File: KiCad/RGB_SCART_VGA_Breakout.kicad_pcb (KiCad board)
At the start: 2 copper layers, 81 x 40.5 mm, 23 parts, among them J1 SCART-F, J11 SJ1-3535NG, J3 DE15_Plug_HighDensity_Mountin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, J4 Conn_01x09, J5 Mounting, J6 Mounting, J7 Mounting, J8 Mounting

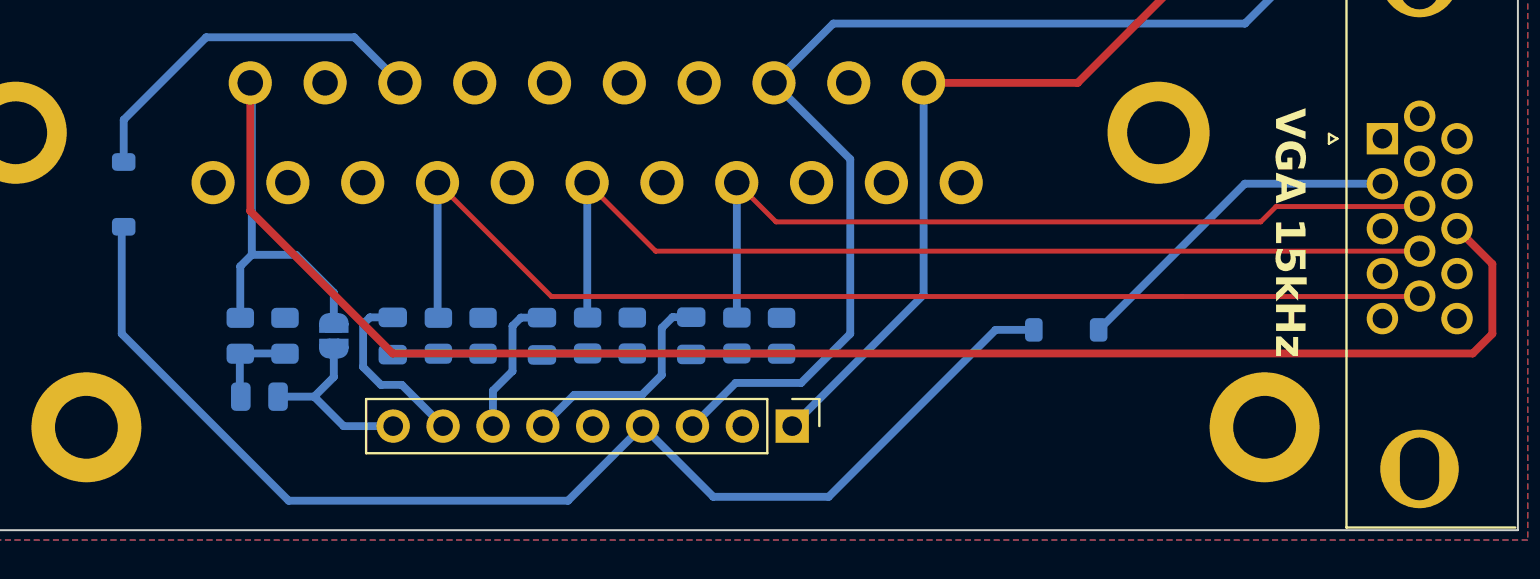
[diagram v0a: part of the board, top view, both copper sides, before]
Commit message: Fixed DE15/VGA connector pinout.
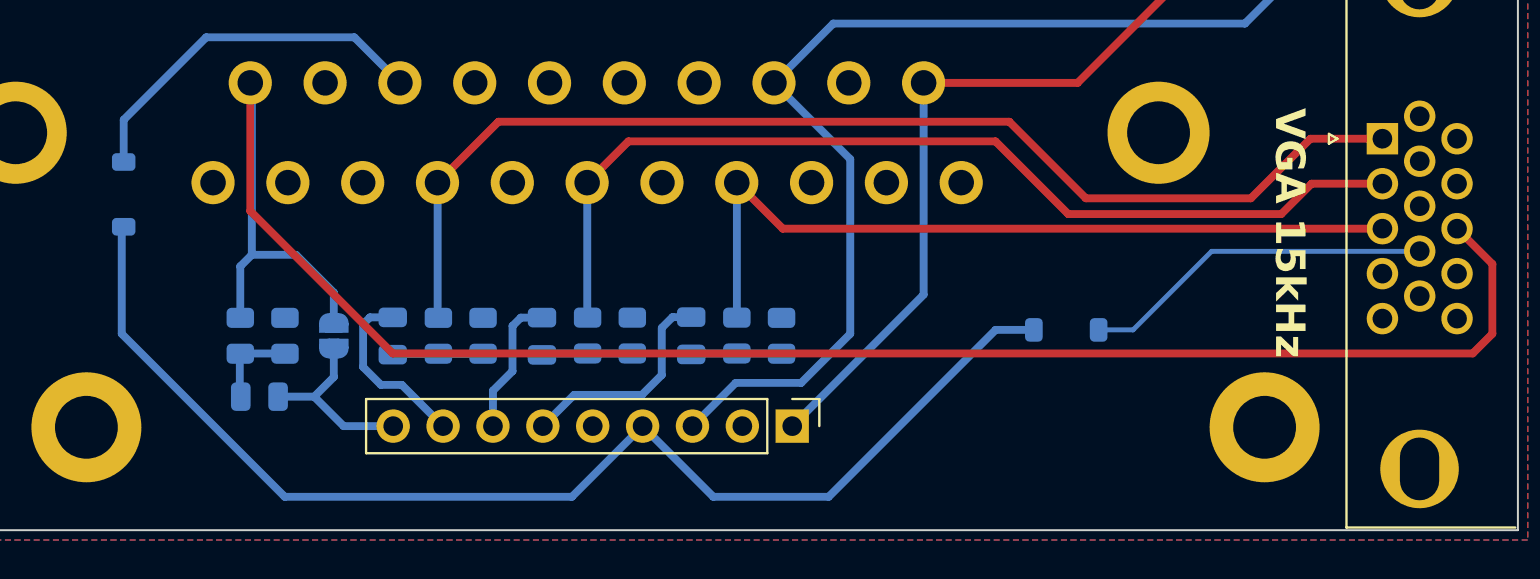
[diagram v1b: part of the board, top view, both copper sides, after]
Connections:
- J3 pad 1: GND -> /RED
- J3 pad 10: /RED -> GND
- J3 pad 12: /VGA_V_SYNC -> unconnected-(J3-Pad12)
- J3 pad 14: unconnected-(J3-Pad14) -> /VGA_V_SYNC
- J3 pad 2: /VGA_5V -> /GREEN
- J3 pad 3: GND -> /BLUE
- J3 pad 4: GND -> unconnected-(J3-Pad4)
- J3 pad 7: unconnected-(J3-Pad7) -> GND
- J3 pad 8: /BLUE -> GND
- J3 pad 9: /GREEN -> /VGA_5V
- J3 pad SH: unconnected-(J3-PadSH)_1 -> (no net)
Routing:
- net /BLUE: track 42.8 -> 40.7 mm
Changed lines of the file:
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@@
 			)
 		)
-		(property "Description" "15-pin D-SUB connector, socket (female), High density (3 columns), Triple Row, Generic, VGA-connector, Mounting Hole"
+		(property "Description" "15-pin D-SUB connector, socket (female), High density (3 columns), Triple Row, Generic, VGA-connector"
 			(at 0 0 90)
 			(layer "F.Fab")
@@
 			(unit
 				(name "A")
-				(pins "6" "1" "7" "2" "8" "3" "9" "4" "10" "5" "SH" "11" "12" "13" "14"
-					"15"
-				)
+				(pins "6" "1" "7" "2" "8" "3" "9" "4" "10" "5" "11" "12" "13" "14" "15")
 			)
 		)
@@
 			(layers "*.Cu" "*.Mask")
 			(remove_unused_layers no)
-			(net "GND")
+			(net "/RED")
 			(pintype "passive")
 		)
@@
 			(layers "*.Cu" "*.Mask")
 			(remove_unused_layers no)
-			(net "/VGA_5V")
+			(net "/GREEN")
 			(pintype "passive")
 		)
@@
 			(layers "*.Cu" "*.Mask")
 			(remove_unused_layers no)
-			(net "GND")
+			(net "/BLUE")
 			(pintype "passive")
 		)
@@
 			(layers "*.Cu" "*.Mask")
 			(remove_unused_layers no)
-			(net "GND")
-			(pintype "passive")
+			(net "unconnected-(J3-Pad4)")
+			(pintype "passive+no_connect")
 		)
 		(pad "5" thru_hole circle
@@
 			(layers "*.Cu" "*.Mask")
 			(remove_unused_layers no)
-			(net "unconnected-(J3-Pad7)")
-			(pintype "passive+no_connect")
+			(net "GND")
+			(pintype "passive")
 		)
 		(pad "8" thru_hole circle
@@
 			(layers "*.Cu" "*.Mask")
 			(remove_unused_layers no)
-			(net "/BLUE")
+			(net "GND")
 			(pintype "passive")
 		)
@@
 			(layers "*.Cu" "*.Mask")
 			(remove_unused_layers no)
-			(net "/GREEN")
+			(net "/VGA_5V")
 			(pintype "passive")
 		)
@@
 			(layers "*.Cu" "*.Mask")
 			(remove_unused_layers no)
-			(net "/RED")
+			(net "GND")
 			(pintype "passive")
 		)
@@
 			(layers "*.Cu" "*.Mask")
 			(remove_unused_layers no)
-			(net "/VGA_V_SYNC")
+			(net "unconnected-(J3-Pad12)")
 			(pintype "passive+no_connect")
 		)
@@
 			(layers "*.Cu" "*.Mask")
 			(remove_unused_layers no)
-			(net "unconnected-(J3-Pad14)")
-			(pintype "passive+no_connect")
+			(net "/VGA_V_SYNC")
+			(pintype "passive")
 		)
 		(pad "15" thru_hole circle
@@
 			(layers "*.Cu" "*.Mask")
 			(remove_unused_layers no)
-			(net "unconnected-(J3-PadSH)")
-			(pintype "passive+no_connect")
 		)
 		(pad "SH" thru_hole circle
@@
 			(layers "*.Cu" "*.Mask")
 			(remove_unused_layers no)
-			(net "unconnected-(J3-PadSH)_1")
-			(pintype "passive+no_connect")
 		)
 		(embedded_fonts no)
@@
 	)
 	(segment
+		(start 191.2 87.8)
+		(end 191.18 87.82)
+		(width 0.25)
+		(layer "F.Cu")
+		(net "GND")
+	)
+	(segment
 		(start 156.679 98.9965)
 		(end 156.679 98.3615)
@@
 	)
 	(segment
+		(start 191.2 92.38)
+		(end 191.18 92.4)
+		(width 0.25)
+		(layer "F.Cu")
+		(net "GND")
+	)
+	(segment
 		(start 156.679 98.9965)
 		(end 156.679 98.933)
@@
 	)
 	(segment
-		(start 147.8245 102.8)
+		(start 148.0245 102.6)
 		(end 151.6245 99)
 		(width 0.4)
@@
 	)
 	(segment
-		(start 125.1 88.95)
-		(end 125.1 94.3)
+		(start 133.4 102.6)
+		(end 148.0245 102.6)
 		(width 0.4)
 		(layer "B.Cu")
@@
 	)
 	(segment
-		(start 125.1 94.3)
-		(end 133.6 102.8)
+		(start 125.1 88.95)
+		(end 125.1 94.3)
 		(width 0.4)
 		(layer "B.Cu")
@@
 	)
 	(segment
-		(start 133.6 102.8)
-		(end 147.8245 102.8)
+		(start 151.599 98.9965)
+		(end 151.599 98.8695)
 		(width 0.4)
 		(layer "B.Cu")
@@
 	)
 	(segment
-		(start 151.599 98.9965)
-		(end 151.599 98.8695)
+		(start 125.1 94.3)
+		(end 133.4 102.6)
 		(width 0.4)
 		(layer "B.Cu")
@@
 	)
 	(segment
-		(start 182.295 86.655)
-		(end 174.85 94.1)
+		(start 144.28 83.5)
+		(end 170.3 83.5)
 		(width 0.4)
-		(layer "B.Cu")
-		(net "/VGA_5V")
+		(layer "F.Cu")
+		(net "/RED")
 	)
 	(segment
-		(start 189.3 86.655)
-		(end 182.295 86.655)
+		(start 141.18 86.6)
+		(end 144.28 83.5)
 		(width 0.4)
-		(layer "B.Cu")
-		(net "/VGA_5V")
-	)
-	(segment
-		(start 191.2 87.8)
-		(end 191.18 87.82)
-		(width 0.25)
 		(layer "F.Cu")
-		(net "/BLUE")
+		(net "/RED")
 	)
 	(segment
-		(start 183.88 87.82)
-		(end 183.1 88.6)
-		(width 0.25)
+		(start 185.635 84.365)
+		(end 189.3 84.365)
+		(width 0.4)
 		(layer "F.Cu")
-		(net "/BLUE")
+		(net "/RED")
 	)
 	(segment
-		(start 158.42 88.6)
-		(end 156.42 86.6)
-		(width 0.25)
+		(start 182.6 87.4)
+		(end 185.635 84.365)
+		(width 0.4)
 		(layer "F.Cu")
-		(net "/BLUE")
+		(net "/RED")
 	)
 	(segment
-		(start 183.1 88.6)
-		(end 158.42 88.6)
-		(width 0.25)
+		(start 174.2 87.4)
+		(end 182.6 87.4)
+		(width 0.4)
 		(layer "F.Cu")
-		(net "/BLUE")
+		(net "/RED")
 	)
 	(segment
-		(start 191.18 87.82)
-		(end 183.88 87.82)
-		(width 0.25)
+		(start 170.3 83.5)
+		(end 174.2 87.4)
+		(width 0.4)
 		(layer "F.Cu")
-		(net "/BLUE")
+		(net "/RED")
 	)
 	(segment
-		(start 156.425 86.605)
-		(end 156.42 86.6)
+		(start 141.185 93.411)
+		(end 141.185 86.605)
 		(width 0.4)
 		(layer "B.Cu")
-		(net "/BLUE")
+		(net "/RED")
 	)
 	(segment
-		(start 156.425 93.4755)
-		(end 156.425 86.605)
+		(start 141.185 86.605)
+		(end 141.18 86.6)
 		(width 0.4)
 		(layer "B.Cu")
-		(net "/BLUE")
+		(net "/RED")
 	)
 	(segment
-		(start 152.29 90.09)
-		(end 148.8 86.6)
-		(width 0.25)
+		(start 169.6 84.5)
+		(end 173.3 88.2)
+		(width 0.4)
 		(layer "F.Cu")
 		(net "/GREEN")
 	)
 	(segment
-		(start 191.2 90.09)
-		(end 152.29 90.09)
-		(width 0.25)
+		(start 148.8 86.6)
+		(end 150.9 84.5)
+		(width 0.4)
+		(layer "F.Cu")
+		(net "/GREEN")
+	)
+	(segment
+		(start 184.15 88.2)
+		(end 185.695 86.655)
+		(width 0.4)
+		(layer "F.Cu")
+		(net "/GREEN")
+	)
+	(segment
+		(start 173.3 88.2)
+		(end 184.15 88.2)
+		(width 0.4)
+		(layer "F.Cu")
+		(net "/GREEN")
+	)
+	(segment
+		(start 150.9 84.5)
+		(end 169.6 84.5)
+		(width 0.4)
+		(layer "F.Cu")
+		(net "/GREEN")
+	)
+	(segment
+		(start 185.695 86.655)
+		(end 189.3 86.655)
+		(width 0.4)
 		(layer "F.Cu")
 		(net "/GREEN")
@@
 	)
 	(segment
-		(start 179.1 92.4)
-		(end 146.98 92.4)
-		(width 0.25)
+		(start 189.3 88.945)
+		(end 158.765 88.945)
+		(width 0.4)
 		(layer "F.Cu")
-		(net "/RED")
+		(net "/BLUE")
 	)
 	(segment
-		(start 191.2 92.38)
-		(end 191.18 92.4)
-		(width 0.25)
+		(start 158.765 88.945)
+		(end 156.42 86.6)
+		(width 0.4)
 		(layer "F.Cu")
-		(net "/RED")
+		(net "/BLUE")
 	)
 	(segment
-		(start 146.98 92.4)
-		(end 141.18 86.6)
+		(start 156.425 86.605)
+		(end 156.42 86.6)
+		(width 0.4)
+		(layer "B.Cu")
+		(net "/BLUE")
+	)
+	(segment
+		(start 156.425 93.4755)
+		(end 156.425 86.605)
+		(width 0.4)
+		(layer "B.Cu")
+		(net "/BLUE")
+	)
+	(segment
+		(start 180.6 90.1)
+		(end 176.6 94.1)
 		(width 0.25)
-		(layer "F.Cu")
-		(net "/RED")
+		(layer "B.Cu")
+		(net "/VGA_5V")
 	)
 	(segment
-		(start 191.18 92.4)
-		(end 179.1 92.4)
+		(start 191.19 90.1)
+		(end 180.6 90.1)
 		(width 0.25)
-		(layer "F.Cu")
-		(net "/RED")
+		(layer "B.Cu")
+		(net "/VGA_5V")
 	)
 	(segment
-		(start 141.185 93.411)
-		(end 141.185 86.605)
-		(width 0.4)
+		(start 191.2 90.09)
+		(end 191.19 90.1)
+		(width 0.25)
 		(layer "B.Cu")
-		(net "/RED")
+		(net "/VGA_5V")
 	)
 	(segment
-		(start 141.185 86.605)
-		(end 141.18 86.6)
-		(width 0.4)
+		(start 176.6 94.1)
+		(end 174.85 94.1)
+		(width 0.25)
 		(layer "B.Cu")
-		(net "/RED")
+		(net "/VGA_5V")
 	)
 	(segment

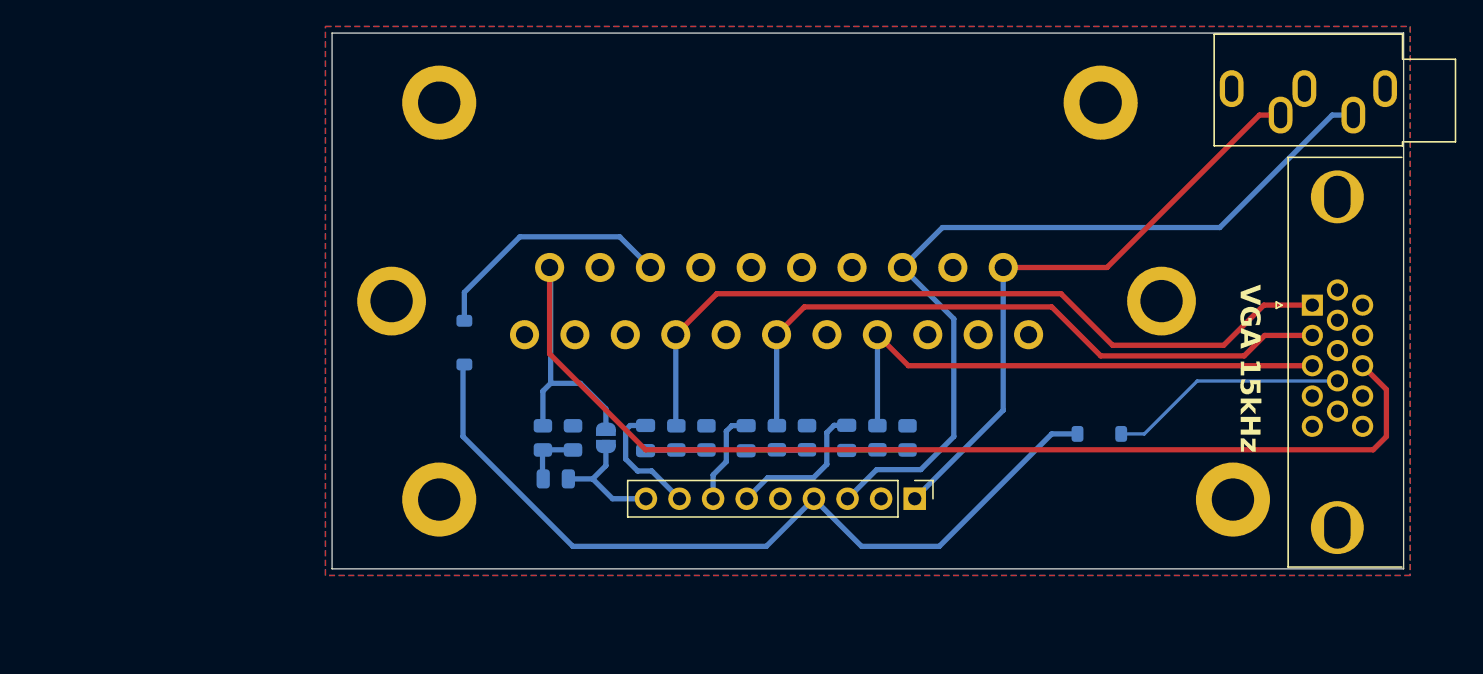
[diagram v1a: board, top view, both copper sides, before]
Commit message: Implement SCART/VGA/S-Video breakout board for JVC TM-1011G RGB/S-Video mod.
MiniDIN 4 pin connector 3D model obtained from https://grabcad.com/library/din-4-pin-connector-2
MiniDIN 4 pin connector footprint edited from MiniDIN 6 pin https://github.com/4x1md/kicad_libraries/blob/master/Custom_Footprints.pretty/Connector_Mini-DIN_Female_6Pin_2rows.kicad_mod
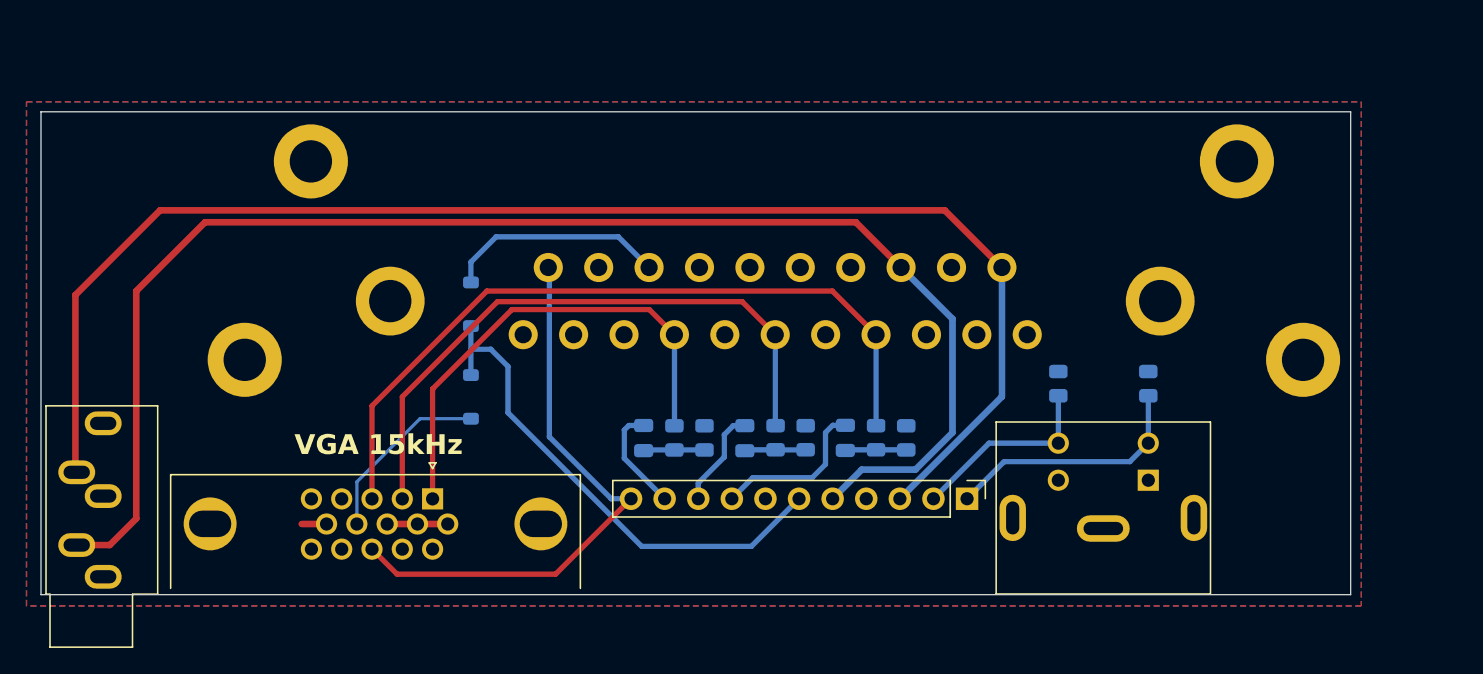
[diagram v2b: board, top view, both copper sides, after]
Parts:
- removed C4: 100nF, Capacitor_SMD:C_0805_2012Metric
- removed JP1: SolderJumper_2_Open, Jumper:SolderJumper-2_P1.3mm_Open_RoundedPad1.0x1.5mm
- removed R4: 30R, Resistor_SMD:R_0805_2012Metric
- removed R5: 75R, Resistor_SMD:R_0805_2012Metric
- added J2: Mini-DIN-4, Connector_Mini-DIN:Connector_Mini-DIN_Female_4Pin, F.Cu at (174.8, 97.6)
- added R10: 510R, Resistor_SMD:R_0805_2012Metric, B.Cu at (170.1, 90.3)
- added R9: 510R, Resistor_SMD:R_0805_2012Metric, B.Cu at (176.9, 90.3)
- J4: footprint Connector_PinHeader_2.54mm:PinHeader_1x09_P2.54mm_Vertical -> Connector_PinHeader_2.54mm:PinHeader_1x11_P2.54mm_Vertical
- moved J11 103.7 mm to (97.9, 104.9), turned to 180 degrees
- moved J3 68.1 mm to (122.8, 99.0), turned to 0 degrees
- moved D1 47.6 mm to (125.7, 91.3), turned to -90 degrees
- moved J6 18.1 mm to (108.6, 88.5)
- moved J5 11.8 mm to (188.6, 88.5)
- moved J8 11.2 mm to (183.6, 73.5)
- moved J7 10.7 mm to (113.6, 73.5)
- moved J4 3.96 mm to (163.2, 99.0)
- moved D2 2.94 mm to (125.7, 84.3)
- moved C1 0.15 mm to (138.8, 94.4)
- moved R1 0.15 mm to (141.1, 94.4)
- moved R8 0.15 mm to (143.4, 94.4)
- moved J1 0.10 mm to (148.7, 84.1)
- moved R3 0.10 mm to (156.3, 94.4)
- moved C2 0.10 mm to (146.4, 94.4)
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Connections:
- J4 pad 1: /AUDIO_R -> /LUMA
- J4 pad 2: GND -> /CHROMA
- J4 pad 3: /AUDIO_L -> /AUDIO_R
- J4 pad 4: /BLANKING -> GND
- J4 pad 5: GND -> /AUDIO_L
- J4 pad 6: /BLUE_OUT -> /BLANKING
- J4 pad 7: /GREEN_OUT -> GND
- J4 pad 8: /RED_OUT -> /BLUE_OUT
- J4 pad 9: /CSYNC_OUT -> /GREEN_OUT
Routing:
- net /AUDIO_R: track 46.0 -> 108.6 mm
- net /CSYNC: track 98.1 -> 43.7 mm
- net /AUDIO_L: track 63.2 -> 109.1 mm
- net /BLANKING: track 62.0 -> 38.2 mm
- net /RED: track 59.1 -> 36.7 mm
- net /LUMA: track 0.00 -> 19.0 mm
- net /BLUE: track 40.7 -> 57.0 mm
- net /CHROMA: track 0.00 -> 14.8 mm
- net /CSYNC_OUT: track 9.47 -> 0.00 mm
- net GND: track 0.76 -> 6.45 mm
- net Net-(C4-Pad2): track 4.33 -> 0.00 mm
- net /VGA_5V: track 18.0 -> 13.8 mm
- net /GREEN: track 50.4 -> 46.7 mm
- net Net-(D2-A): track 18.9 -> 16.8 mm
- net /RED_OUT: track 9.41 -> 8.11 mm
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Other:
- board size 81 x 40.5 mm -> 99 x 36.5 mm
- board text added: "C"
- board text added: "Y"

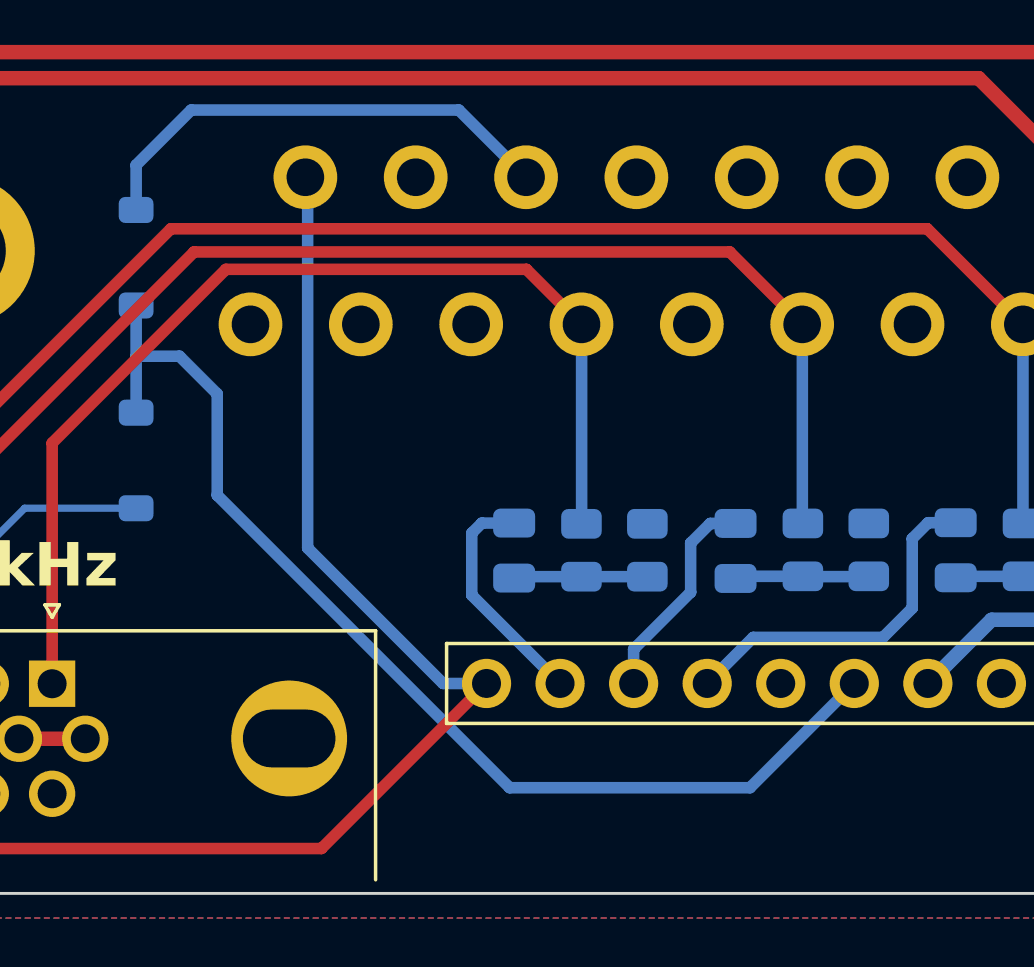
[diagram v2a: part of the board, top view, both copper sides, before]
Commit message: Added blanking voltage divider / pulldown resistors with description. Expanded RGB load / voltage divider resistors description.
PCB version 1.1.
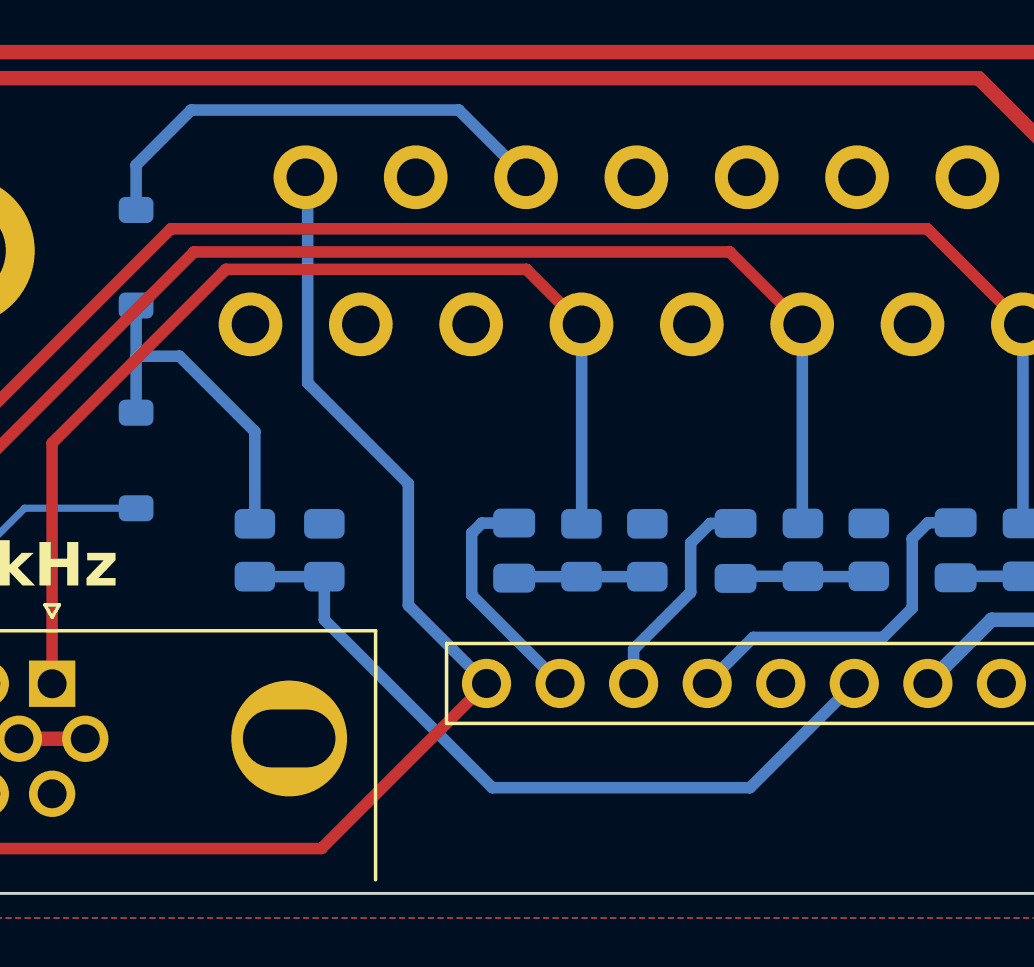
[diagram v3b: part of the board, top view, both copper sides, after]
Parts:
- added R11: 1K, Resistor_SMD:R_0805_2012Metric, B.Cu at (129.8, 94.4)
- added R12: 2K3, Resistor_SMD:R_0805_2012Metric, B.Cu at (132.2, 94.4)
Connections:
- J4 pad 6: /BLANKING -> /BLANKING_DIV
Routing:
- net /BLANKING: track 38.2 -> 12.1 mm
- net /BLANKING_DIV: track 0.00 -> 26.1 mm
- net /CSYNC: track 43.7 -> 42.8 mm
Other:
- board text added: "V.1.1"
